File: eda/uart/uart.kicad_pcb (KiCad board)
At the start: 2 copper layers, 133.3 x 85.2 mm, 54 parts, among them J1 UART, J2 Conn_02x25_Odd_Even, U1 74HCT08, U10 74HCT574, U11 74HCT595, U12 74HCT595, U13 CD74HCT40105E, U14 CD74HCT40105E, U15 74HCT00, U16 74HCT74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

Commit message: Branch of uart to v1
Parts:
- removed D1: 1N4001, Diode_THT:D_DO-41_SOD81_P10.16mm_Horizontal
- removed R1: 10K, Resistor_THT:R_Axial_DIN0207_L6.3mm_D2.5mm_P7.62mm_Horizontal
- added H3: MountingHole_Pad, MountingHole:MountingHole_2.5mm_Pad_Via, F.Cu at (255.0, 52.3)
- added H4: MountingHole_Pad, MountingHole:MountingHole_2.5mm_Pad_Via, F.Cu at (255.0, 143.3)
- added H5: MountingHole_Pad, MountingHole:MountingHole_2.5mm_Pad_Via, F.Cu at (164.0, 52.4)
- added H6: MountingHole_Pad, MountingHole:MountingHole_2.5mm_Pad_Via, F.Cu at (164.2, 143.4)
- H1, H2: value MountingHole -> MountingHole_Pad; footprint MountingHole:MountingHole_2.5mm -> MountingHole:MountingHole_2.5mm_Pad_Via
- J2: footprint Connector_PinHeader_2.54mm:PinHeader_2x25_P2.54mm_Horizontal -> Connector_PinHeader_2.54mm:PinHeader_2x25_P2.54mm_Vertical
- moved C7 190.6 mm to (236.6, 88.4), turned to 180 degrees
- moved JP8 182.7 mm to (252.8, 115.3), turned to 0 degrees
- moved U6 181.9 mm to (230.1, 93.0), turned to 0 degrees
- moved JP7 180.7 mm to (252.8, 112.8), turned to 0 degrees
- moved JP6 178.8 mm to (252.8, 110.2), turned to 0 degrees
- moved C8 177.2 mm to (246.9, 59.4)
- moved JP5 176.9 mm to (252.8, 107.7), turned to 0 degrees
- moved JP4 175.1 mm to (252.8, 105.2), turned to 0 degrees
- moved JP3 173.3 mm to (252.8, 102.6), turned to 0 degrees
- moved JP2 171.6 mm to (252.8, 100.1), turned to 0 degrees
- moved U5 170.4 mm to (230.6, 64.0), turned to 0 degrees
- moved JP1 170.0 mm to (252.8, 97.5), turned to 0 degrees
- moved U3 165.5 mm to (238.5, 122.7)
- moved C21 162.4 mm to (205.2, 136.7)
- moved U16 156.6 mm to (205.7, 115.8)
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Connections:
- U11 pad 14: /Expansion header/D6 -> Net-(U11-SER)
- U12 pad 9: unconnected-(U12-QH'-Pad9) -> Net-(U11-SER)
- U13 pad 4: /recieve/FIFO Recieve/D0 -> /Expansion header/D0
- U13 pad 5: /recieve/FIFO Recieve/D1 -> /Expansion header/D1
- U13 pad 6: /recieve/FIFO Recieve/D2 -> /Expansion header/D2
- U13 pad 7: /recieve/FIFO Recieve/D3 -> /Expansion header/D3
- U14 pad 4: /recieve/FIFO Recieve/D4 -> /Expansion header/D4
- U14 pad 5: /recieve/FIFO Recieve/D5 -> /Expansion header/D5
- U14 pad 6: /recieve/FIFO Recieve/D6 -> /Expansion header/D6
- U14 pad 7: /recieve/FIFO Recieve/D7 -> /Expansion header/D7
- U17 pad 5: GND -> VCC
- U2 pad 13: GND -> /address_decode/~{RecieveEnable}
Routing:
- net VCC: track 810.9 -> 180.9 mm, vias 4 -> 0
- net /clock/UartClock: track 208.4 -> 29.9 mm, vias 3 -> 0
- net /Expansion header/~{CS}: track 118.1 -> 17.8 mm
- net /transmit/FIFO Transmit/DOR: track 94.4 -> 0.00 mm, vias 3 -> 0
- net /transmit/TX: track 94.4 -> 0.00 mm
- net /Expansion header/Clock: track 83.1 -> 0.00 mm, vias 2 -> 0
- net /recieve/Reset: track 89.9 -> 14.9 mm, vias 2 -> 0
- net /recieve/RX: track 87.3 -> 37.1 mm, vias 5 -> 0
- net /recieve/FIFO Recieve/D6: track 42.4 -> 0.00 mm
- net /Expansion header/A1: track 40.2 -> 0.00 mm, vias 2 -> 0
- net /Expansion header/A0: track 39.1 -> 0.00 mm, vias 2 -> 0
- net /transmit/~{ClockEnable}: track 66.7 -> 28.0 mm
- net /recieve/FIFO Recieve/D5: track 34.5 -> 0.00 mm
- net /recieve/FIFO Recieve/D4: track 34.5 -> 0.00 mm
- net /transmit/FIFO Transmit/Q0: track 35.0 -> 5.08 mm, vias 1 -> 0
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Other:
- board size 133.3 x 85.2 mm -> 230 x 100 mm
- board text added: "A0"
- board text added: "A1"
- board text added: "A10"
- board text added: "A11"
- board text added: "A12"
- board text added: "A13"
- board text added: "A14"
- board text added: "A15"
- board text added: "A2"
- board text added: "A3"
- board text added: "A4"
- board text added: "A5"
- board text added: "A6"
- board text added: "A7"
- board text added: "A8"
- board text added: "A9"
- board text added: "CLK"
- board text added: "D0"
- board text added: "D1"
- board text added: "D2"
- board text added: "D3"
- board text added: "D4"
- board text added: "D5"
- board text added: "D6"
- board text added: "D7"
- board text added: "GND"
- board text added: "IO0"
- board text added: "IO1"
- board text added: "IO2"
- board text added: "IO3"
- board text added: "IO4"
- board text added: "IO5"
- board text added: "IO6"
- board text added: "IO7"
- board text added: "R~{W}"
- board text added: "VCC"
- board text added: "~{DMA}"
- board text added: "~{IRQ}"
- board text added: "~{NMI}"
- board text added: "~{RST}"

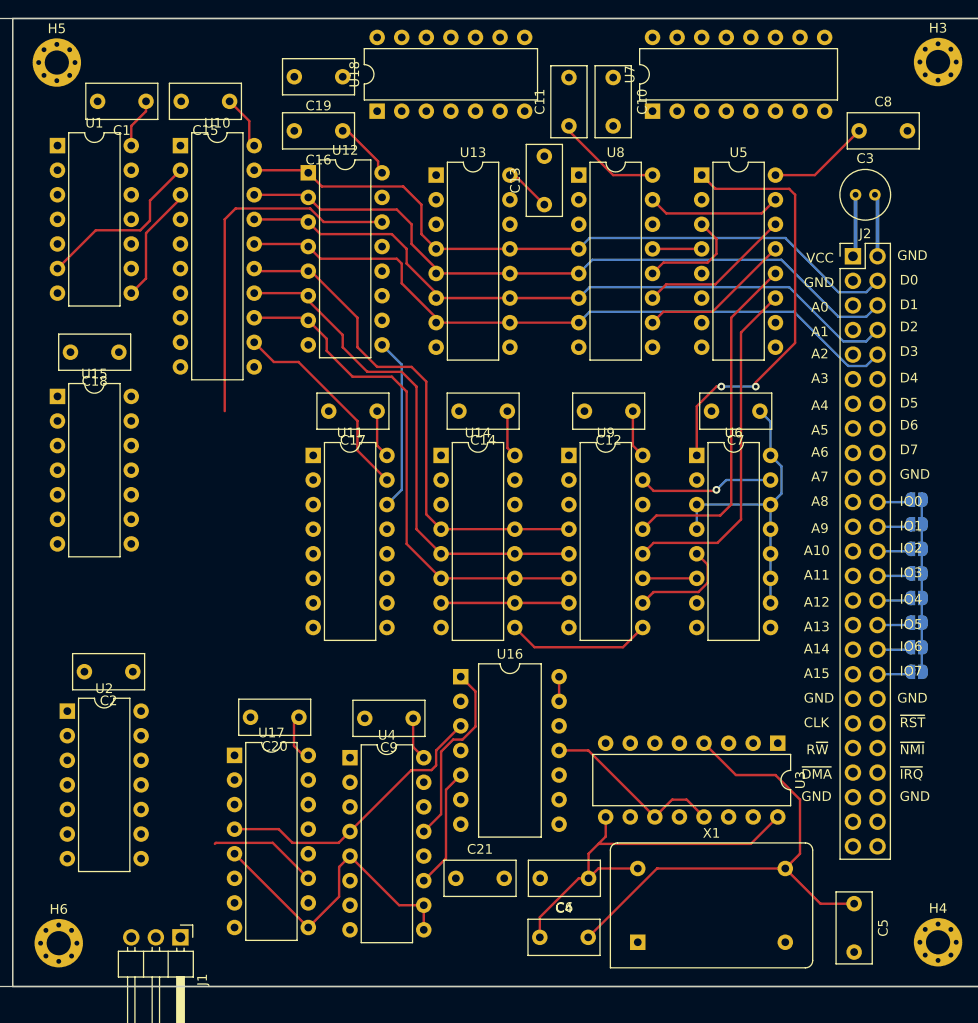
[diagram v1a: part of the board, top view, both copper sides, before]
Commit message: Normalize cap size
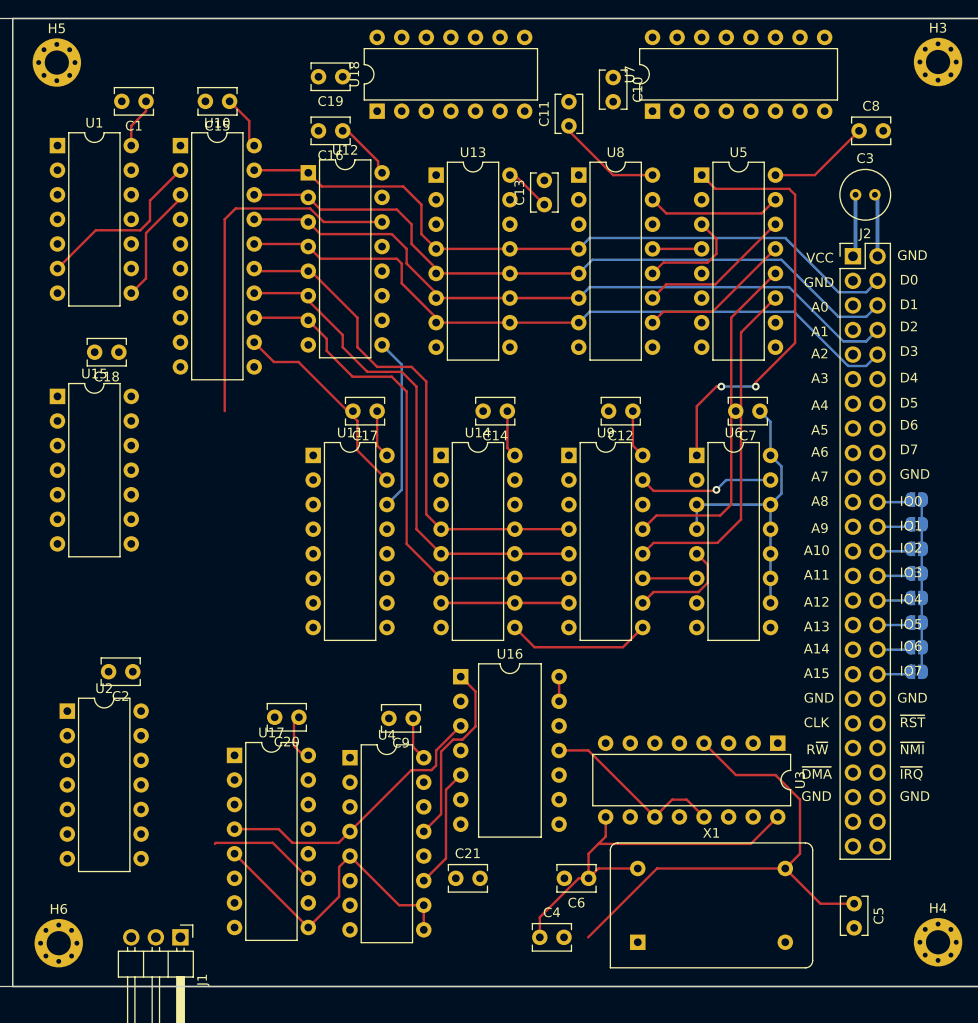
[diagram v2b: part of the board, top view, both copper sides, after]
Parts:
- C1, C10, C11, C12, C13, C14, C15, C16, C17, C18, C19, C2, C20, C21, C4, C5, C6, C7, C8, C9: footprint Capacitor_THT:C_Rect_L7.2mm_W3.5mm_P5.00mm_FKS2_FKP2_MKS2_MKP2 -> Capacitor_THT:C_Disc_D3.8mm_W2.6mm_P2.50mm

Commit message: Uart eda work
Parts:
- removed H1, H2: MountingHole_Pad, MountingHole:MountingHole_2.5mm_Pad_Via
- added C22: 0.1uf, Capacitor_THT:C_Disc_D3.8mm_W2.6mm_P2.50mm, F.Cu at (91.0, 87.3)
- added JP9: IRQ Disconnect, Connector_PinHeader_2.54mm:PinHeader_1x02_P2.54mm_Vertical, F.Cu at (167.1, 126.0)
- added U19: 74HCT74, Package_DIP:DIP-14_W7.62mm, F.Cu at (88.2, 91.8)
- J1: value UART -> RX/TX Con; footprint Connector_PinHeader_2.54mm:PinHeader_1x03_P2.54mm_Horizontal -> Connector_PinHeader_2.54mm:PinHeader_1x04_P2.54mm_Horizontal
- moved C2 90.8 mm to (81.3, 109.1)
- moved C14 90.4 mm to (120.4, 82.3)
- moved C20 90.2 mm to (99.1, 113.8)
- moved C12 90.1 mm to (133.6, 82.3)
- moved C17 90.1 mm to (107.2, 82.8)
- moved C9 89.8 mm to (111.3, 113.9)
- moved C3 88.8 mm to (158.0, 59.8)
- moved C6 88.8 mm to (130.4, 130.4)
- moved C8 88.8 mm to (158.3, 53.2)
- moved H3 88.8 mm to (166.5, 46.1)
- moved H4 88.8 mm to (166.5, 137.0)
- moved H6 88.8 mm to (75.6, 137.1)
- moved JP1 88.8 mm to (164.3, 91.3)
- moved JP2 88.8 mm to (164.3, 93.9)
- moved JP3 88.8 mm to (164.3, 96.4)
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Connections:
- net Net-(U7A-E) renamed /address_decode/~{DeviceEnable}
- J1 pad 1: GND -> unconnected-(J1-Pin_1-Pad1)
- J1 pad 2: /recieve/RX -> /transmit/TX
- J1 pad 3: /transmit/TX -> /recieve/RX
- U10 pad 2: /transmit/InputBufferFull -> /recieve/RecieveBufferFull
- U10 pad 3: /recieve/RecieveBufferFull -> Net-(U10-D1)
- U10 pad 4: /recieve/DataAvailable -> GND
- U10 pad 8: GND -> /transmit/InputBufferFull
- U10 pad 9: GND -> /recieve/DataAvailable
- U15 pad 4: GND -> /recieve/DataAvailable
- U15 pad 5: GND -> /address_decode/IrqActive
- U15 pad 6: unconnected-(U15-Pad6) -> Net-(U19B-~{S})
- U17 pad 15: GND -> VCC
- U7 pad 7: unconnected-(U7A-O3-Pad7) -> Net-(U19A-C)
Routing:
- net /Expansion header/~{RST}: track 0.00 -> 174.6 mm, vias 0 -> 4
- net Net-(U7A-O0): track 0.00 -> 164.0 mm, vias 0 -> 2
- net /address_decode/~{DeviceEnable}: track 0.00 -> 129.9 mm, vias 0 -> 2
- net /transmit/TX: track 0.00 -> 120.8 mm, vias 0 -> 1
- net VCC: track 180.9 -> 61.7 mm
- net /Expansion header/Clock: track 0.00 -> 118.7 mm, vias 0 -> 3
- net Net-(U18-Pad2): track 0.00 -> 118.3 mm, vias 0 -> 2
- net Net-(U19A-C): track 0.00 -> 107.9 mm, vias 0 -> 2
- net /Expansion header/R~{W}: track 0.00 -> 102.4 mm, vias 0 -> 2
- net Net-(U9-DOR): track 0.00 -> 101.4 mm, vias 0 -> 2
- net /transmit/FIFO Transmit/DOR: track 0.00 -> 96.0 mm, vias 0 -> 1
- net /Expansion header/~{CS}: track 17.8 -> 112.4 mm, vias 0 -> 2
- net /clock/UartClock: track 29.9 -> 122.7 mm, vias 0 -> 3
- net Net-(JP9-B): track 0.00 -> 86.0 mm, vias 0 -> 4
- net /address_decode/TransmitEnable: track 0.00 -> 73.6 mm, vias 0 -> 1
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- added copper zone on In2.Cu, net GND
- added copper zone on In1.Cu, net VCC
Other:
- board size 230 x 100 mm -> 100 x 100 mm
- copper layers 2 -> 4

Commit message: UART routing pass 1
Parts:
- removed C17: 0.1uf, Capacitor_THT:C_Disc_D3.8mm_W2.6mm_P2.50mm
- removed U11: 74HCT595, Package_DIP:DIP-16_W7.62mm
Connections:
- U12 pad 1: /Expansion header/D0 -> /Expansion header/D6
- U12 pad 15: unconnected-(U12-QA-Pad15) -> /Expansion header/D7
- U12 pad 2: /Expansion header/D1 -> /Expansion header/D5
- U12 pad 3: /Expansion header/D2 -> /Expansion header/D4
- U12 pad 5: /Expansion header/D4 -> /Expansion header/D2
- U12 pad 6: /Expansion header/D5 -> /Expansion header/D1
- U12 pad 7: /Expansion header/D6 -> /Expansion header/D0
- U17 pad 1: GND -> VCC
- U17 pad 15: VCC -> GND
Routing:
- net /address_decode/~{RecieveEnable}: track 7.02 -> 103.1 mm, vias 0 -> 2
- net Net-(U8-DIR): track 0.00 -> 83.0 mm, vias 0 -> 5
- net Net-(U9-DIR): track 0.00 -> 77.7 mm, vias 0 -> 3
- net Net-(U14-DOR): track 0.00 -> 76.2 mm, vias 0 -> 5
- net /clock/UartClock: track 122.7 -> 191.4 mm
- net Net-(U14-DIR): track 0.00 -> 53.5 mm, vias 0 -> 4
- net /recieve/Reset: track 82.6 -> 130.8 mm, vias 3 -> 5
- net Net-(U13-DIR): track 0.00 -> 38.9 mm, vias 0 -> 2
- net /recieve/FIFO Recieve/SI: track 64.7 -> 100.6 mm, vias 1 -> 3
- net /Expansion header/D7: track 99.5 -> 135.1 mm, vias 2 -> 4
- net Net-(U5-DS): track 0.00 -> 34.7 mm, vias 0 -> 1
- net /transmit/~{ClockEnable}: track 76.7 -> 109.7 mm, vias 1 -> 2
- net /address_decode/TransmitEnable: track 73.6 -> 106.1 mm, vias 1 -> 2
- net /Expansion header/D5: track 119.2 -> 142.0 mm, vias 1 -> 3
- net Net-(U12-~{SRCLR}): track 72.0 -> 94.6 mm, vias 0 -> 2
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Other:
- board text added: "Niklas Hedlund, 2024"
- board text added: "Project Wrass, UART v1.0 115200 - N81"

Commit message: Cleanup uart
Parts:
- moved JP9 5.11 mm to (167.6, 120.9)
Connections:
- J2 pad 47: unconnected-(J2-Pin_47-Pad47) -> /Expansion header/AudioL
- J2 pad 48: unconnected-(J2-Pin_48-Pad48) -> /Expansion header/~{ExtRomCs}
- J2 pad 49: unconnected-(J2-Pin_49-Pad49) -> /Expansion header/AudioR
- J2 pad 50: unconnected-(J2-Pin_50-Pad50) -> VCC
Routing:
- net (no net): track 70.0 -> 0.00 mm
- net VCC: track 61.7 -> 0.88 mm
- net GND: track 6.46 -> 0.38 mm
- net Net-(JP9-B): track 86.0 -> 84.4 mm
- net /Expansion header/~{IRQ}: track 9.59 -> 8.00 mm
- net /Expansion header/D1: track 84.4 -> 83.6 mm
- net /Expansion header/D4: track 134.5 -> 133.8 mm
- net /Expansion header/D0: track 124.0 -> 123.4 mm
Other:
- board text added: "NC"
- board text added: "RX"
- board text added: "TX"

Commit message: Touchups before ordering
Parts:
- X1: value 1.8xx -> 1.8432 Mhz
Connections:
- J1 pad 2: /transmit/TX -> /recieve/RX
- J1 pad 3: /recieve/RX -> /transmit/TX
- U10 pad 11: /Expansion header/Clock -> Net-(U10-Cp)
- U7 pad 11: unconnected-(U7B-O1-Pad11) -> Net-(U10-Cp)
- U7 pad 14: GND -> /Expansion header/Clock
- U7 pad 15: VCC -> GND
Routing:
- net /Expansion header/Clock: track 118.7 -> 219.0 mm, vias 3 -> 5
- net Net-(U10-Cp): track 0.00 -> 94.9 mm, vias 0 -> 2
- net /transmit/TX: track 121.2 -> 124.8 mm, vias 1 -> 2
- net /recieve/RX: track 104.2 -> 103.6 mm
- removed copper zone on B.Cu, net GND
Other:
- board text added: "Project Wrass, UART v1.0 115200, 8-N-1"
- board text removed: "Project Wrass, UART v1.0 115200 - N81"

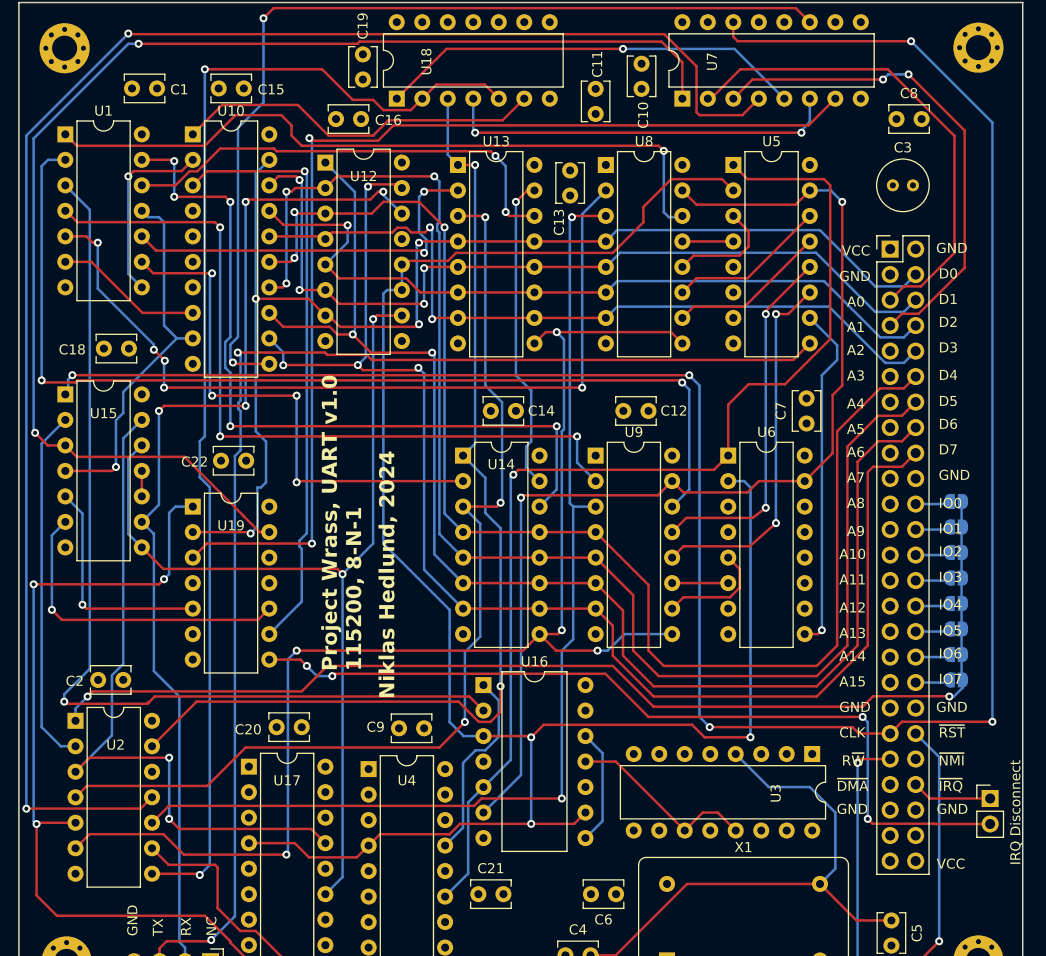
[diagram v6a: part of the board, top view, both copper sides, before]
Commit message: Uart board to v1.1...make bodges permanent :(
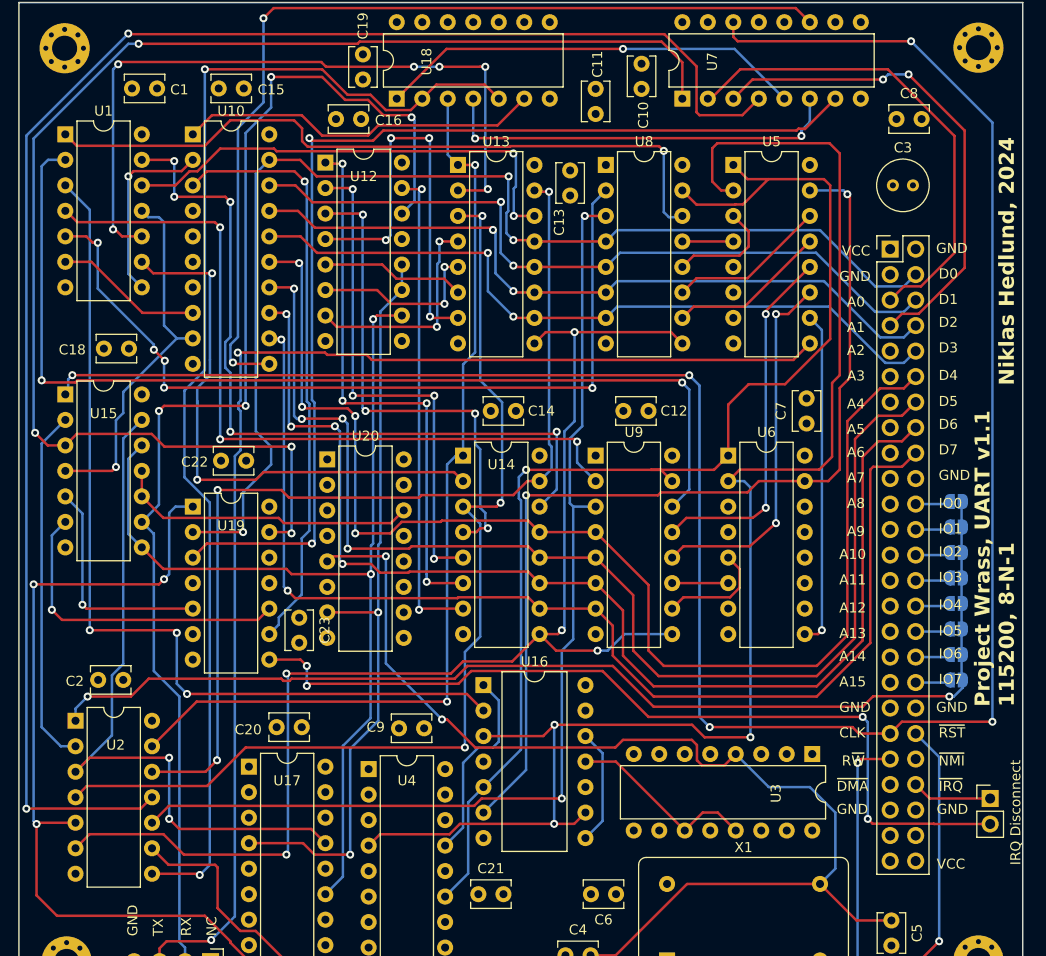
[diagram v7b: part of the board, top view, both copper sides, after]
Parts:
- added C23: 0.1uf, Capacitor_THT:C_Disc_D3.8mm_W2.6mm_P2.50mm, F.Cu at (98.8, 102.9)
- added U20: 74HCT193, Package_DIP:DIP-16_W7.62mm, F.Cu at (101.6, 87.1)
- X1: value 1.8432 Mhz -> 1.8xx
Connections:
- net Net-(U15-Pad10) renamed /clock/~{InRecieveMode}
- U12 pad 1: /Expansion header/D6 -> /recieve/ID6
- U12 pad 11: /clock/UartClock -> /clock/UartRecieveClock
- U12 pad 12: /clock/UartClock -> /clock/UartRecieveClock
- U12 pad 15: /Expansion header/D7 -> /recieve/ID7
- U12 pad 2: /Expansion header/D5 -> /recieve/ID5
- U12 pad 3: /Expansion header/D4 -> /recieve/ID4
- U12 pad 4: /Expansion header/D3 -> /recieve/ID3
- U12 pad 5: /Expansion header/D2 -> /recieve/ID2
- U12 pad 6: /Expansion header/D1 -> /recieve/ID1
- U12 pad 7: /Expansion header/D0 -> /recieve/ID0
- U13 pad 4: /Expansion header/D0 -> /recieve/ID0
- U13 pad 5: /Expansion header/D1 -> /recieve/ID1
- U13 pad 6: /Expansion header/D2 -> /recieve/ID2
- U13 pad 7: /Expansion header/D3 -> /recieve/ID3
- U14 pad 4: /Expansion header/D4 -> /recieve/ID4
- U14 pad 5: /Expansion header/D5 -> /recieve/ID5
- U14 pad 6: /Expansion header/D6 -> /recieve/ID6
- U14 pad 7: /Expansion header/D7 -> /recieve/ID7
- U17 pad 4: /clock/UartClock -> /clock/UartRecieveClock
- U2 pad 12: unconnected-(U2-Pad12) -> /recieve/FIFO Recieve/SO
- U8 pad 15: /transmit/~{ClockEnable} -> /transmit/~{LatchShiftRegisters}
- U9 pad 15: /transmit/~{ClockEnable} -> /transmit/~{LatchShiftRegisters}
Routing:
- net /clock/UartRecieveClock: track 0.00 -> 76.6 mm, vias 0 -> 2
- net /recieve/FIFO Recieve/SO: track 31.5 -> 97.9 mm, vias 1 -> 3
- net Net-(U20-UP): track 54.5 -> 112.3 mm, vias 0 -> 2
- net /recieve/ID6: track 0.00 -> 55.3 mm, vias 0 -> 4
- net /recieve/ID5: track 0.00 -> 50.7 mm, vias 0 -> 4
- net /recieve/ID4: track 0.00 -> 49.1 mm, vias 0 -> 4
- net /recieve/ID7: track 0.00 -> 48.5 mm, vias 0 -> 2
- net /clock/UartClock: track 191.4 -> 148.8 mm
- net /recieve/ID3: track 0.00 -> 41.3 mm, vias 0 -> 4
- net Net-(U13-DIR): track 38.9 -> 72.0 mm, vias 2 -> 6
- net /clock/~{InRecieveMode}: track 2.54 -> 30.3 mm
- net /recieve/RX: track 103.6 -> 125.9 mm
- net /recieve/ID0: track 0.00 -> 22.0 mm, vias 0 -> 2
- net /Expansion header/D5: track 141.7 -> 122.0 mm, vias 3 -> 4
- net /Expansion header/D7: track 135.1 -> 115.9 mm, vias 4 -> 2
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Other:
- board text added: "Project Wrass, UART v1.1 115200, 8-N-1"
- board text removed: "Project Wrass, UART v1.0 115200, 8-N-1"
